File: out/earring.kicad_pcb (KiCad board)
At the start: 4 copper layers, 30.5 x 35.8 mm, 123 parts, among them J1 USB-C, SW1 BOOTSEL, SW2 PWR, U1 RP2350A, U2 LGS4056H, U3 NCP730-3.3, U4 TPS22913, U5 USBLC6-2P6, U6 LSM6DS3TR-C, U7 W25Q16JVUXIQ, Y1 12MHz

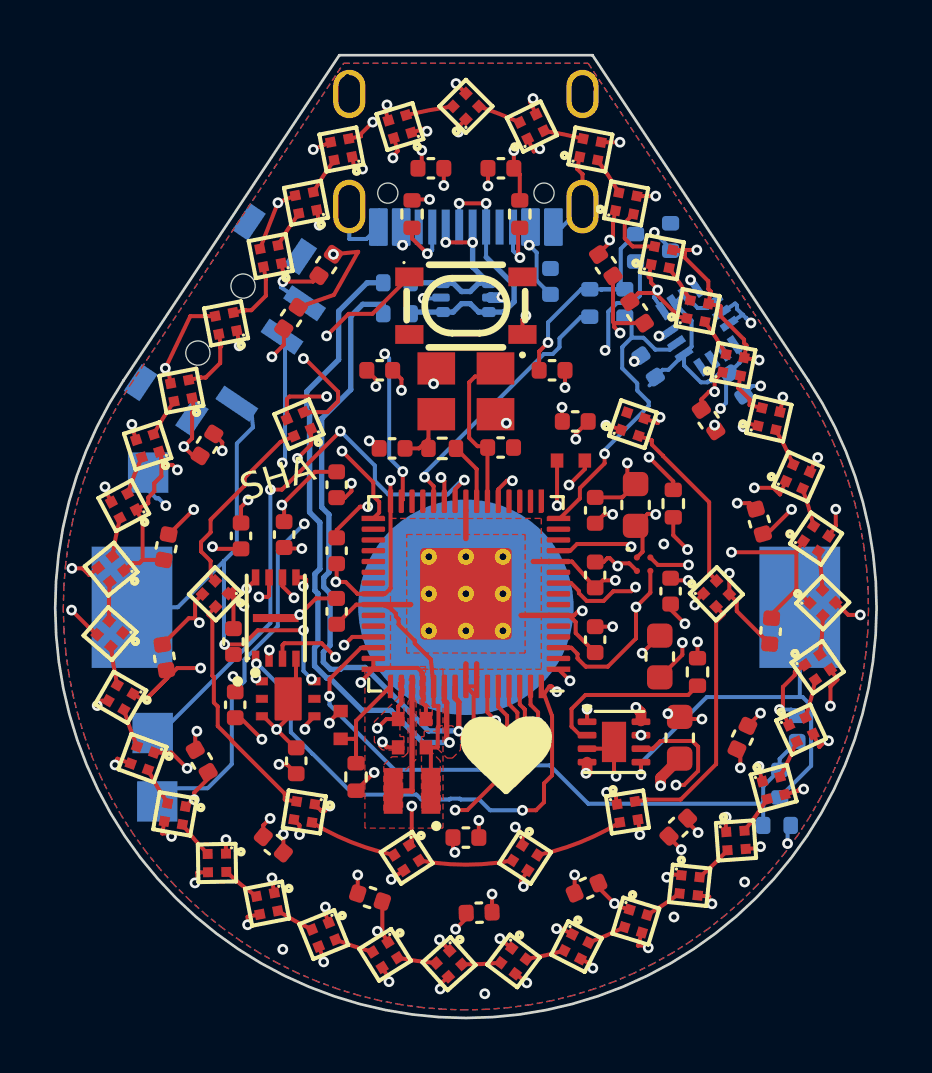
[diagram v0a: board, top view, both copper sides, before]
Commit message: Back-port hand edits: silk art into the generator, VBUS via move
Board (Sequoia's hand edits, Aug 7): VBUS tip via moved off the B4A9
tie pad (102.35,86.55)->(102.2,87.01) with In2/B.Cu trunk rework, CC2
via (102.01,87.02)->(101.59,86.98), a VLED/LED_D38 via+track cleanup
on the west ring, and five new front texts (Sequoia Hope / Alexander
/ Be Gay / Do Crimes / Love Everyone, 0.8mm) replacing "SHA".
DRC: 0 errors / 0 unconnected, no dangling.

Generator:
- NEW scripts/silk_art.py: heart outline (141 pts, embedded), the two
  back URL arcs, and the five hand texts - called from gen_board.py so
  rebuilds reproduce all silk. Verified: applied to a bare board it
  matches the tracked board's 43 art texts exactly and the heart to
  rounding.
- route.py: committed VBUS via updated to Sequoia's new spot
  (2.20,-12.99). CC2/VLED vias were router-placed, nothing to port.

Co-Authored-By: Claude Fable 5 <noreply@anthropic.com>
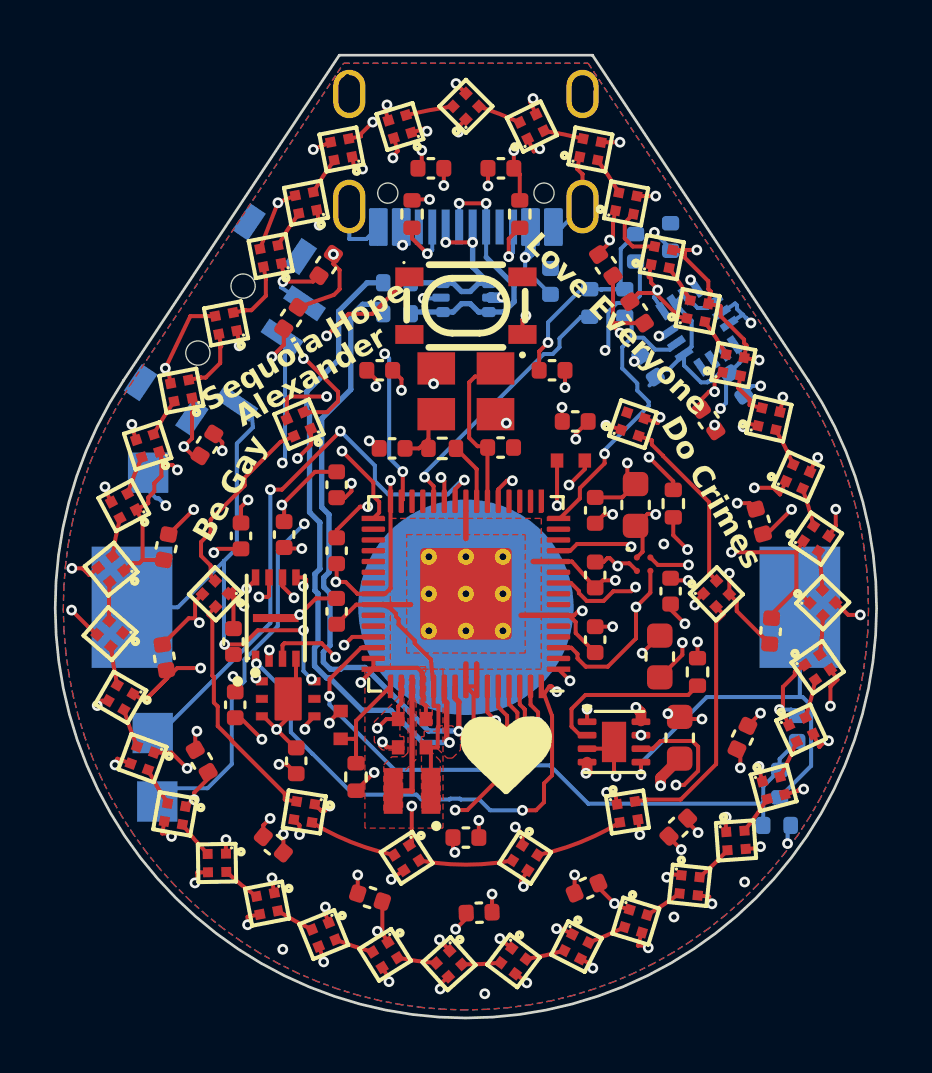
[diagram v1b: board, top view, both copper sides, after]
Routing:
- net VLED: track 79.8 -> 78.7 mm
- net VBUS: track 63.0 -> 63.9 mm
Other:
- board text added: "Alexander"
- board text added: "Be Gay"
- board text added: "Do Crimes"
- board text added: "Love Everyone"
- board text added: "Sequoia Hope"
- board text removed: "SHA"

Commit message: ORDERED REV: commit fab exports as sent to JLCPCB
This is the revision ordered on 2026-08-08. out/production/ (gerber
zip, BOM, CPL/positions, designators, IPC netlist) is the exact
export package uploaded for the order, generated 2026-08-07 19:32
from the board file committed here (verified byte-identical to the
pre-export backup).

Board changes since last commit: silk text "Do Crimes" -> "Do Crime"
and a minor net-8 F.Cu reroute near (91.2, 99.5).

.gitignore now tracks out/production/ (excluding backups/).

Co-Authored-By: Claude Fable 5 <noreply@anthropic.com>
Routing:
- net GND: track 115.3 -> 114.4 mm
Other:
- board text added: "Do Crime"
- board text removed: "Do Crimes"
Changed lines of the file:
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@@
 		)
 	)
-	(gr_text "Do Crimes"
+	(gr_text "Do Crime"
 		(at 107.15 93.24 300)
 		(layer "F.SilkS")
@@
 	)
 	(segment
-		(start 91.1808 99.4916)
-		(end 91.3796 99.2858)
-		(width 0.15)
-		(layer "F.Cu")
-		(net 8)
-	)
-	(segment
 		(start 99.7251 82.3532)
 		(end 99.7251 82.1558)
@@
 	)
 	(segment
-		(start 91.3796 99.578817)
-		(end 91.758885 99.958102)
-		(width 0.15)
-		(layer "F.Cu")
-		(net 8)
-	)
-	(segment
 		(start 104.3265 83.9163)
 		(end 104.1349 83.7247)
@@
 	)
 	(segment
+		(start 91.1808 99.4916)
+		(end 91.647302 99.958102)
+		(width 0.15)
+		(layer "F.Cu")
+		(net 8)
+	)
+	(segment
 		(start 97.9745 82.3757)
 		(end 98.46 82.2273)
@@
 	)
 	(segment
+		(start 91.3689 100.4511)
+		(end 91.758885 100.061115)
+		(width 0.15)
+		(layer "F.Cu")
+		(net 8)
+	)
+	(segment
 		(start 107.7493 89.1816)
 		(end 107.7493 89.0518)
@@
 	)
 	(segment
-		(start 91.3796 99.2858)
-		(end 91.3796 99.578817)
-		(width 0.15)
-		(layer "F.Cu")
-		(net 8)
-	)
-	(segment
 		(start 98.6509 84.8554)
 		(end 98.0346 84.8554)
@@
 	)
 	(segment
+		(start 91.647302 99.958102)
+		(end 91.758885 99.958102)
+		(width 0.15)
+		(layer "F.Cu")
+		(net 8)
+	)
+	(segment
 		(start 105.3384 86.3632)
 		(end 105.4622 86.2394)
@@
 	)
 	(segment
+		(start 91.3689 100.7928)
+		(end 91.3689 100.4511)
+		(width 0.15)
+		(layer "F.Cu")
+		(net 8)
+	)
+	(segment
 		(start 90.4298 106.1239)
 		(end 90.4298 106.3643)
@@
 	)
 	(segment
-		(start 91.3689 99.6529)
-		(end 91.3689 100.7928)
-		(width 0.15)
-		(layer "F.Cu")
-		(net 8)
-	)
-	(segment
 		(start 110.5407 96.1333)
 		(end 110.762 96.3546)
@@
 	)
 	(segment
-		(start 88.6124 94.223)
-		(end 88.6926 94.4699)
+		(start 91.758885 100.061115)
+		(end 91.758885 99.958102)
 		(width 0.15)
 		(layer "F.Cu")
@@
 	)
 	(segment
-		(start 91.3796 99.6422)
-		(end 91.3689 99.6529)
+		(start 88.6124 94.223)
+		(end 88.6926 94.4699)
 		(width 0.15)
 		(layer "F.Cu")
@@
 		(width 0.15)
 		(layer "F.Cu")
-		(net 8)
-	)
-	(segment
-		(start 91.3796 99.2858)
-		(end 91.3796 99.6422)
-		(width 0.15)
-		(layer "F.Cu")

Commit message: Battery clip: swap BT1 to MYOUNG MY-2032-12-R (C964834), flat-foot SMD
Ordered rev shipped the QIJEY CR2032-W footprint without its mandatory
Ø3.5/3.6 through-holes (feet are bent for reverse-side soldering; holes
impossible under the front LED ring). The MY-2032-12-R is the flat-foot
architectural fix: copper kept IDENTICAL to the ordered rev (pads
10.9..13.9, feet land 10.65..12.05 -> 1.15mm on-pad), BT1 swapped
surgically on out/earring.kicad_pcb (pads/nets verified, DRC 0 err).
New BAT_MY2032_12R generator in gen_footprints.py; easyeda2kicad wrl
(already 0.1-inch units, no scale bake). Rev-2 TODO stays: stretch pads
inward toward the datasheet land (2.4x6.1 at +-11.35).

Co-Authored-By: Claude Fable 5 <noreply@anthropic.com>
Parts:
- BT1: footprint earring:BAT_CR2032_W -> earring:BAT_MY2032_12R
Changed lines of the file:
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@@
 		(embedded_fonts no)
-	)
-	(footprint "earring:BAT_CR2032_W"
-		(layer "B.Cu")
-		(at 100 100 180)
-		(descr "QIJEY CR2032-W SMD coin cell retainer clip, LCSC C70373. Clip=+ (pin1), center pad=- (pin2). Cell + marking faces out.")
-		(tags "battery LIR2032 CR2032 retainer")
-		(property "Reference" "BT1"
-			(at 0 13.2 0)
-			(layer "B.SilkS")
-			(hide yes)
-			(effects
-				(font
-					(size 0.5 0.5)
-					(thickness 0.1)
-				)
-				(justify mirror)
-			)
-		)
-		(property "Value" "LIR2032"
-			(at 0 -13.2 0)
-			(layer "B.Fab")
-			(hide yes)
-			(effects
-				(font
-					(size 1 1)
-					(thickness 0.15)
-				)
-				(justify mirror)
-			)
-		)
-		(property "Datasheet" ""
-			(at 0 0 0)
-			(layer "B.Fab")
-			(hide yes)
-			(effects
-				(font
-					(size 1.27 1.27)
-					(thickness 0.15)
-				)
-				(justify mirror)
-			)
-		)
-		(property "Description" ""
-			(at 0 0 0)
-			(layer "B.Fab")
-			(hide yes)
-			(effects
-				(font
-					(size 1.27 1.27)
-					(thickness 0.15)
-				)
-				(justify mirror)
-			)
-		)
-		(property "LCSC" "C70373"
-			(at 0 0 0)
-			(layer "B.SilkS")
-			(hide yes)
-			(effects
-				(font
-					(size 1.27 1.27)
-					(thickness 0.15)
-				)
-				(justify mirror)
-			)
-		)
-		(sheetname "/")
-		(sheetfile "earring.kicad_sch")
-		(attr smd)
-		(fp_circle
-			(center 0 0)
-			(end 10.15 0)
-			(stroke
-				(width 0.15)
-				(type default)
-			)
-			(fill no)
-			(layer "B.SilkS")
-		)
-		(fp_rect
-			(start 10.5 3.4)
-			(end 14.1 -3.4)
-			(stroke
-				(width 0.05)
-				(type default)
-			)
-			(fill no)
-			(layer "B.CrtYd")
-		)
-		(fp_rect
-			(start -14.1 3.4)
-			(end -10.5 -3.4)
-			(stroke
-				(width 0.05)
-				(type default)
-			)
-			(fill no)
-			(layer "B.CrtYd")
-		)
-		(fp_circle
-			(center 0 0)
-			(end 10.4 0)
-			(stroke
-				(width 0.05)
-				(type default)
-			)
-			(fill no)
-			(layer "B.CrtYd")
-		)
-		(fp_text user "+"
-			(at 0 11.5 0)
-			(layer "B.SilkS")
-			(effects
-				(font
-					(size 1 1)
-					(thickness 0.2)
-				)
-				(justify mirror)
-			)
-		)
-		(pad "1" smd rect
-			(at -12.4 0 180)
-			(size 3 4.5)
-			(layers "B.Cu" "B.Mask" "B.Paste")
-			(net 71 "VBATT")
-			(pinfunction "1")
-			(pintype "passive")
-		)
-		(pad "1" smd rect
-			(at 12.4 0 180)
-			(size 3 4.5)
-			(layers "B.Cu" "B.Mask" "B.Paste")
-			(net 71 "VBATT")
-			(pinfunction "1")
-			(pintype "passive")
-		)
-		(pad "2" smd circle
-			(at 0 0 180)
-			(size 8 8)
-			(layers "B.Cu" "B.Mask")
-			(net 8 "GND")
-			(pinfunction "2")
-			(pintype "passive")
-		)
-		(embedded_fonts no)
-		(model "${KIPRJMOD}/../library/3d/ee.3dshapes/BAT-SMD_CR2032_C70373.wrl"
-			(offset
-				(xyz 0 0 0)
-			)
-			(scale
-				(xyz 1 1 1)
-			)
-			(rotate
-				(xyz 0 0 180)
-			)
-		)
 	)
 	(footprint "earring:C_0402_1005Metric"
@@
 			(offset
 				(xyz 0 0 0)
+			)
+			(scale
+				(xyz 1 1 1)
+			)
+			(rotate
+				(xyz 0 0 0)
+			)
+		)
+	)
+	(footprint "earring:BAT_MY2032_12R"
+		(layer "B.Cu")
+		(at 100 100 180)
+		(descr "MYOUNG MY-2032-12-R SMD coin cell retainer clip, LCSC C964834. Clip=+ (pin1), center pad=- (pin2). Flat feet, no thru-holes. Copper identical to BAT_CR2032_W (ordered rev).")
+		(tags "battery LIR2032 CR2032 retainer")
+		(property "Reference" "BT1"
+			(at 0 13.2 0)
+			(layer "B.SilkS")
+			(hide yes)
+			(effects
+				(font
+					(size 1 1)
+					(thickness 0.15)
+				)
+				(justify mirror)
+			)
+		)
+		(property "Value" "LIR2032"
+			(at 0 -13.2 0)
+			(layer "B.Fab")
+			(hide yes)
+			(effects
+				(font
+					(size 1 1)
+					(thickness 0.15)
+				)
+				(justify mirror)
+			)
+		)
+		(property "Datasheet" ""
+			(at 0 0 0)
+			(layer "B.Fab")
+			(hide yes)
+			(effects
+				(font
+					(size 1.27 1.27)
+					(thickness 0.15)
+				)
+				(justify mirror)
+			)
+		)
+		(property "Description" ""
+			(at 0 0 0)
+			(layer "B.Fab")
+			(hide yes)
+			(effects
+				(font
+					(size 1.27 1.27)
+					(thickness 0.15)
+				)
+				(justify mirror)
+			)
+		)
+		(property "LCSC" "C964834"
+			(at 0 0 0)
+			(layer "B.SilkS")
+			(hide yes)
+			(effects
+				(font
+					(size 1.27 1.27)
+					(thickness 0.15)
+				)
+			)
+		)
+		(attr smd)
+		(fp_circle
+			(center 0 0)
+			(end 10.15 0)
+			(stroke
+				(width 0.15)
+				(type default)
+			)
+			(fill no)
+			(layer "B.SilkS")
+		)
+		(fp_rect
+			(start 10.5 3.4)
+			(end 14.1 -3.4)
+			(stroke
+				(width 0.05)
+				(type default)
+			)
+			(fill no)
+			(layer "B.CrtYd")
+		)
+		(fp_rect
+			(start -14.1 3.4)
+			(end -10.5 -3.4)
+			(stroke
+				(width 0.05)
+				(type default)
+			)
+			(fill no)
+			(layer "B.CrtYd")
+		)
+		(fp_circle
+			(center 0 0)
+			(end 10.4 0)
+			(stroke
+				(width 0.05)
+				(type default)
+			)
+			(fill no)
+			(layer "B.CrtYd")
+		)
+		(fp_text user "+"
+			(at 0 11.5 0)
+			(layer "B.SilkS")
+			(effects
+				(font
+					(size 1 1)
+					(thickness 0.2)
+				)
+				(justify mirror)
+			)
+		)
+		(pad "1" smd rect
+			(at -12.4 0 180)
+			(size 3 4.5)
+			(layers "B.Cu" "B.Mask" "B.Paste")
+			(net 71 "VBATT")
+		)
+		(pad "1" smd rect
+			(at 12.4 0 180)
+			(size 3 4.5)
+			(layers "B.Cu" "B.Mask" "B.Paste")
+			(net 71 "VBATT")
+		)
+		(pad "2" smd circle
+			(at 0 0 180)
+			(size 8 8)
+			(layers "B.Cu" "B.Mask")
+			(net 8 "GND")
+		)
+		(embedded_fonts no)
+		(model "${KIPRJMOD}/../library/3d/ee.3dshapes/BAT-SMD_MY-2032-12_C964834.wrl"
+			(offset
+				(xyz 0 0 0)
